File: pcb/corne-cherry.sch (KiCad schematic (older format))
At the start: 146 parts, among them J1 MJ-4PP-9, J2 OLED, J3 MJ-4PP-9, J4 OLED, J5 Conn_01x01_Male, J6 Conn_01x01_Male, P1 Conn_01x03, P3 Conn_01x03, SW1 SW_PUSH, SW10 SW_PUSH, SW11 SW_PUSH, SW12 SW_PUSH, SW13 SW_PUSH, SW14 SW_PUSH, SW15 SW_PUSH, SW16 SW_PUSH, SW17 SW_PUSH, SW18 SW_PUSH, SW19 SW_PUSH, SW2 SW_PUSH, SW20 SW_PUSH, SW21 SW_PUSH, SW22 SW_PUSH, SW23 SW_PUSH, SW24 SW_PUSH, SW25 SW_PUSH, SW26 SW_PUSH, SW27 SW_PUSH, SW28 SW_PUSH, SW29 SW_PUSH, SW3 SW_PUSH, SW30 SW_PUSH, SW31 SW_PUSH, SW32 SW_PUSH, SW33 SW_PUSH, SW34 SW_PUSH, SW35 SW_PUSH, SW36 SW_PUSH, SW37 SW_PUSH, SW38 SW_PUSH, SW39 SW_PUSH, SW4 SW_PUSH, SW40 SW_PUSH, SW41 SW_PUSH, SW42 SW_PUSH, SW43 Rotary_Encoder_Switch, SW44 Rotary_Encoder_Switch, SW5 SW_PUSH, SW6 SW_PUSH, SW7 SW_PUSH, SW8 SW_PUSH, SW9 SW_PUSH, U1 ProMicro, U2 ProMicro

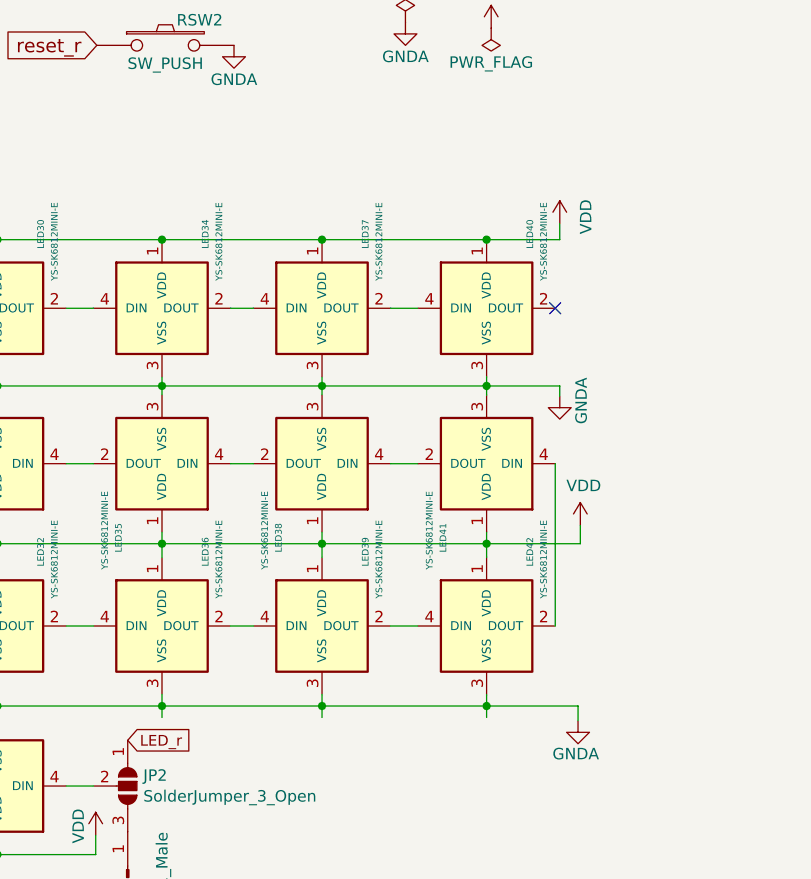
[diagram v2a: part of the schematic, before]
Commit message: Clean up schematic
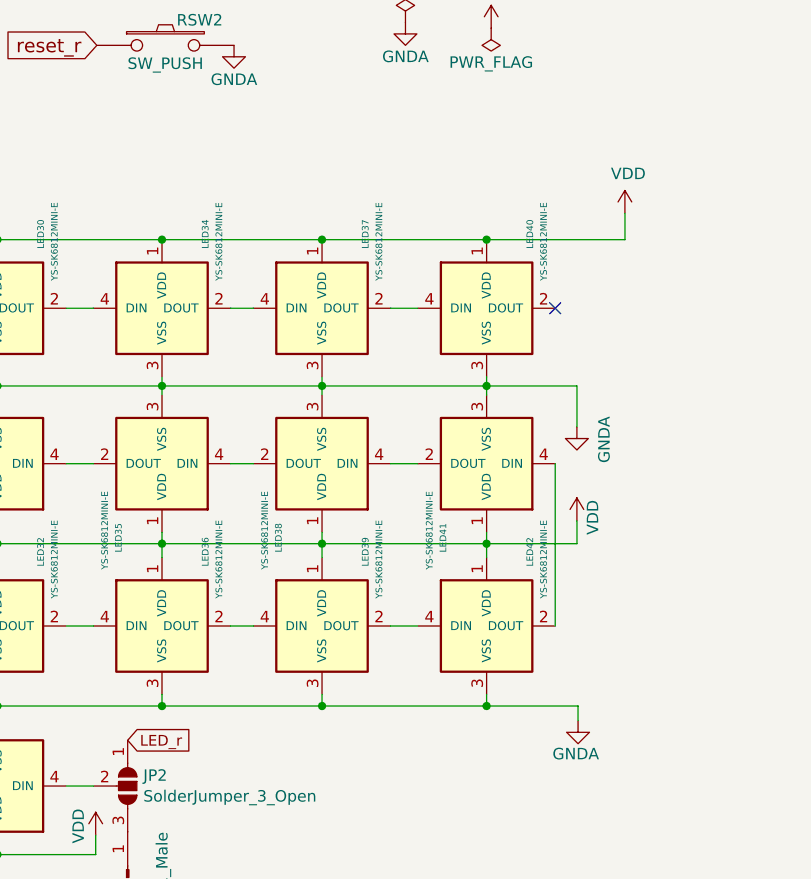
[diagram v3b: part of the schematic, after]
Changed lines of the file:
@@
 Wire Wire Line
 	7930 5730 7810 5730
-NoConn ~ 11380 5050
 $Comp
 L Connector:Conn_01x01_Male J6
@@
 Connection ~ 11080 5390
 Wire Wire Line
-	11080 5390 11400 5390
-Wire Wire Line
 	11080 5430 11080 5390
 Wire Wire Line
@@
 	8230 6790 7510 6790
 Wire Wire Line
-	11080 6840 11080 6790
-Wire Wire Line
 	11080 6740 11080 6790
 Connection ~ 11080 6790
@@
 Connection ~ 11080 6080
 Wire Wire Line
-	11080 6080 11490 6080
-Wire Wire Line
 	11080 6140 11080 6080
 Wire Wire Line
@@
 Wire Wire Line
 	10360 6080 11080 6080
-Wire Wire Line
-	10360 6840 10360 6790
 Connection ~ 10360 6790
 Wire Wire Line
@@
 Wire Wire Line
 	9960 6440 10060 6440
-Wire Wire Line
-	9660 6840 9660 6790
 Connection ~ 9660 6790
 Wire Wire Line
@@
 Wire Wire Line
 	9240 7140 9360 7140
-$Comp
-L power:VDD #PWR0112
-U 1 1 60837821
-P 11490 6000
-F 0 "#PWR0112" H 11490 5850 50  0001 C CNN
-F 1 "VDD" H 11505 6173 50  0000 C CNN
-F 2 "" H 11490 6000 50  0001 C CNN
-F 3 "" H 11490 6000 50  0001 C CNN
-	1    11490 6000
-	1    0    0    -1
-$EndComp
 $Comp
 L power:GNDA #PWR0115
@@
 	0    1    1    0
 $EndComp
-$Comp
-L power:VDD #PWR0114
-U 1 1 60838250
-P 11400 4680
-F 0 "#PWR0114" H 11400 4530 50  0001 C CNN
-F 1 "VDD" V 11515 4710 50  0000 C CNN
-F 2 "" H 11400 4680 50  0001 C CNN
-F 3 "" H 11400 4680 50  0001 C CNN
-	1    11400 4680
-	1    0    0    -1
-$EndComp
 Wire Wire Line
 	5360 7410 5360 7325
@@
 Wire Wire Line
 	11480 6855 11480 6790
-Wire Wire Line
-	11490 6080 11490 6000
-Connection ~ 11080 4750
-Wire Wire Line
-	11080 4750 11400 4750
+$Comp
+L Device:Rotary_Encoder_Switch SW43
+U 1 1 6078866B
+P 3135 785
+F 0 "SW43" V 3089 1015 50  0000 L CNN
+F 1 "Rotary_Encoder_Switch" V 3180 1015 50  0000 L CNN
+F 2 "Keebio-Parts:RotaryEncoder_EC11-no-legs" H 2985 945 50  0001 C CNN
+F 3 "~" H 3135 1045 50  0001 C CNN
+	1    3135 785
+	1    0    0    -1
+$EndComp
+Wire Wire Line
+	2835 785  2420 785
+Wire Wire Line
+	2420 785  2420 885
+$Comp
+L power:GND #PWR0119
+U 1 1 60823858
+P 2420 885
+F 0 "#PWR0119" H 2420 635 50  0001 C CNN
+F 1 "GND" H 2425 712 50  0000 C CNN
+F 2 "" H 2420 885 50  0001 C CNN
+F 3 "" H 2420 885 50  0001 C CNN
+	1    2420 885
+	1    0    0    -1
+$EndComp
+Text GLabel 2835 685  0    50   Input ~ 0
+ENC_A
+Text GLabel 2835 885  0    50   Input ~ 0
+ENC_B
+Text GLabel 2475 2275 2    50   Input ~ 0
+ENC_B
+Text GLabel 2475 2175 2    50   Input ~ 0
+ENC_A
+Wire Wire Line
+	3435 885  3435 1275
+Wire Wire Line
+	3435 1275 3600 1275
+Connection ~ 3600 1275
+Wire Wire Line
+	3600 1275 3600 2475
+Wire Wire Line
+	3435 685  4200 685
+Wire Wire Line
+	4200 685  4200 1275
+Connection ~ 4200 1275
+Text GLabel 9905 2150 2    50   Input ~ 0
+ENC_A_R
+Text GLabel 9905 2250 2    50   Input ~ 0
+ENC_B_R
+$Comp
+L Device:Rotary_Encoder_Switch SW44
+U 1 1 60786552
+P 11045 930
+F 0 "SW44" H 11045 1297 50  0000 C CNN
+F 1 "Rotary_Encoder_Switch" H 11045 1206 50  0000 C CNN
+F 2 "Keebio-Parts:RotaryEncoder_EC11-no-legs" H 10895 1090 50  0001 C CNN
+F 3 "~" H 11045 1190 50  0001 C CNN
+	1    11045 930
+	1    0    0    -1
+$EndComp
+Text GLabel 10745 1030 0    50   Input ~ 0
+ENC_B_R
+Text GLabel 10745 830  0    50   Input ~ 0
+ENC_A_R
+Wire Wire Line
+	10745 930  10150 930
+Wire Wire Line
+	10150 930  10150 1030
+$Comp
+L power:GNDA #PWR0120
+U 1 1 607DCD43
+P 10150 1030
+F 0 "#PWR0120" H 10150 780 50  0001 C CNN
+F 1 "GNDA" V 10060 1020 50  0000 C CNN
+F 2 "" H 10150 1030 50  0001 C CNN
+F 3 "" H 10150 1030 50  0001 C CNN
+	1    10150 1030
+	1    0    0    -1
+$EndComp
+Wire Wire Line
+	11345 830  12175 830
+Wire Wire Line
+	12175 830  12175 1400
+Connection ~ 12175 1400
+Wire Wire Line
+	11345 1030 11345 1400
+Wire Wire Line
+	11345 1400 11575 1400
+Connection ~ 11575 1400
+Wire Wire Line
+	11575 1400 11575 2600
 Wire Wire Line
 	10360 4750 11080 4750
@@
 	1    0    0    -1
 $EndComp
-$Comp
-L power:GNDA #PWR0116
-U 1 1 6087A621
-P 11400 5435
-F 0 "#PWR0116" H 11400 5185 50  0001 C CNN
-F 1 "GNDA" V 11495 5415 50  0000 C CNN
-F 2 "" H 11400 5435 50  0001 C CNN
-F 3 "" H 11400 5435 50  0001 C CNN
-	1    11400 5435
-	1    0    0    -1
-$EndComp
-Wire Wire Line
-	11400 5390 11400 5435
-Wire Wire Line
-	11400 4750 11400 4680
-$Comp
-L Device:Rotary_Encoder_Switch SW43
-U 1 1 6078866B
-P 3135 785
-F 0 "SW43" V 3089 1015 50  0000 L CNN
-F 1 "Rotary_Encoder_Switch" V 3180 1015 50  0000 L CNN
-F 2 "Keebio-Parts:RotaryEncoder_EC11-no-legs" H 2985 945 50  0001 C CNN
-F 3 "~" H 3135 1045 50  0001 C CNN
-	1    3135 785
-	1    0    0    -1
-$EndComp
-Wire Wire Line
-	2835 785  2420 785
-Wire Wire Line
-	2420 785  2420 885
-$Comp
-L power:GND #PWR0119
-U 1 1 60823858
-P 2420 885
-F 0 "#PWR0119" H 2420 635 50  0001 C CNN
-F 1 "GND" H 2425 712 50  0000 C CNN
-F 2 "" H 2420 885 50  0001 C CNN
-F 3 "" H 2420 885 50  0001 C CNN
-	1    2420 885
-	1    0    0    -1
-$EndComp
-Text GLabel 2835 685  0    50   Input ~ 0
-ENC_A
-Text GLabel 2835 885  0    50   Input ~ 0
-ENC_B
-Text GLabel 2475 2275 2    50   Input ~ 0
-ENC_B
-Text GLabel 2475 2175 2    50   Input ~ 0
-ENC_A
-Wire Wire Line
-	3435 885  3435 1275
-Wire Wire Line
-	3435 1275 3600 1275
-Connection ~ 3600 1275
-Wire Wire Line
-	3600 1275 3600 2475
-Wire Wire Line
-	3435 685  4200 685
-Wire Wire Line
-	4200 685  4200 1275
-Connection ~ 4200 1275
-Text GLabel 9905 2150 2    50   Input ~ 0
-ENC_A_R
-Text GLabel 9905 2250 2    50   Input ~ 0
-ENC_B_R
-$Comp
-L Device:Rotary_Encoder_Switch SW44
-U 1 1 60786552
-P 11045 930
-F 0 "SW44" H 11045 1297 50  0000 C CNN
-F 1 "Rotary_Encoder_Switch" H 11045 1206 50  0000 C CNN
-F 2 "Keebio-Parts:RotaryEncoder_EC11-no-legs" H 10895 1090 50  0001 C CNN
-F 3 "~" H 11045 1190 50  0001 C CNN
-	1    11045 930
-	1    0    0    -1
-$EndComp
-Text GLabel 10745 1030 0    50   Input ~ 0
-ENC_B_R
-Text GLabel 10745 830  0    50   Input ~ 0
-ENC_A_R
-Wire Wire Line
-	10745 930  10150 930
-Wire Wire Line
-	10150 930  10150 1030
-$Comp
-L power:GNDA #PWR0120
-U 1 1 607DCD43
-P 10150 1030
-F 0 "#PWR0120" H 10150 780 50  0001 C CNN
-F 1 "GNDA" V 10060 1020 50  0000 C CNN
-F 2 "" H 10150 1030 50  0001 C CNN
-F 3 "" H 10150 1030 50  0001 C CNN
-	1    10150 1030
-	1    0    0    -1
-$EndComp
-Wire Wire Line
-	11345 830  12175 830
-Wire Wire Line
-	12175 830  12175 1400
-Connection ~ 12175 1400
-Wire Wire Line
-	11345 1030 11345 1400
-Wire Wire Line
-	11345 1400 11575 1400
-Connection ~ 11575 1400
-Wire Wire Line
-	11575 1400 11575 2600
+NoConn ~ 11380 5050
+Wire Wire Line
+	11080 6080 11475 6080
+Wire Wire Line
+	11475 6080 11475 5980
+$Comp
+L power:VDD #PWR0112
+U 1 1 60DCBB52
+P 11475 5980
+F 0 "#PWR0112" H 11475 5830 50  0001 C CNN
+F 1 "VDD" V 11545 5995 50  0000 C CNN
+F 2 "" H 11475 5980 50  0001 C CNN
+F 3 "" H 11475 5980 50  0001 C CNN
+	1    11475 5980
+	1    0    0    -1
+$EndComp
+Wire Wire Line
+	11080 5390 11475 5390
+Wire Wire Line
+	11475 5390 11475 5570
+$Comp
+L power:GNDA #PWR0114
+U 1 1 60DF6BE8
+P 11475 5570
+F 0 "#PWR0114" H 11475 5320 50  0001 C CNN
+F 1 "GNDA" V 11595 5515 50  0000 C CNN
+F 2 "" H 11475 5570 50  0001 C CNN
+F 3 "" H 11475 5570 50  0001 C CNN
+	1    11475 5570
+	1    0    0    -1
+$EndComp
+Wire Wire Line
+	11080 4750 11685 4750
+Wire Wire Line
+	11685 4750 11685 4635
+Connection ~ 11080 4750
+$Comp
+L power:VDD #PWR0116
+U 1 1 60E14086
+P 11685 4635
+F 0 "#PWR0116" H 11685 4485 50  0001 C CNN
+F 1 "VDD" H 11700 4808 50  0000 C CNN
+F 2 "" H 11685 4635 50  0001 C CNN
+F 3 "" H 11685 4635 50  0001 C CNN
+	1    11685 4635
+	1    0    0    -1
+$EndComp
 $EndSCHEMATC

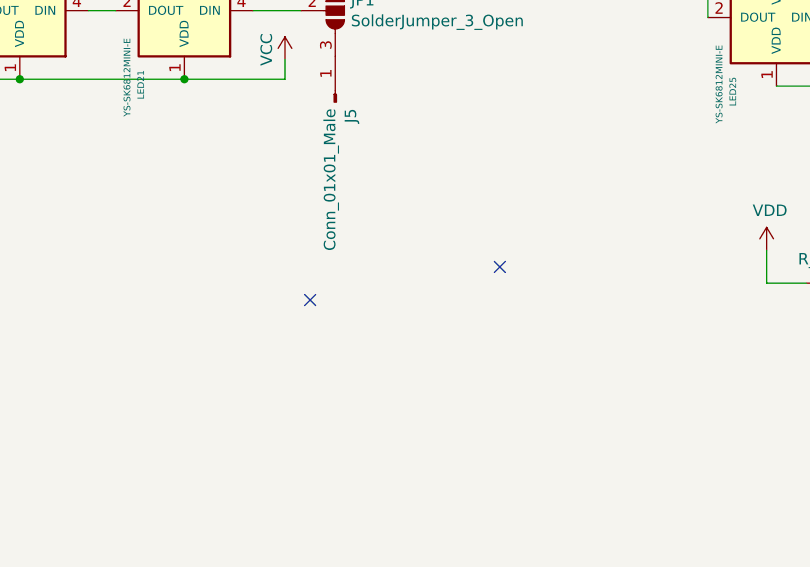
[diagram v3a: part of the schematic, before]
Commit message: change trace position - too close too mousebites
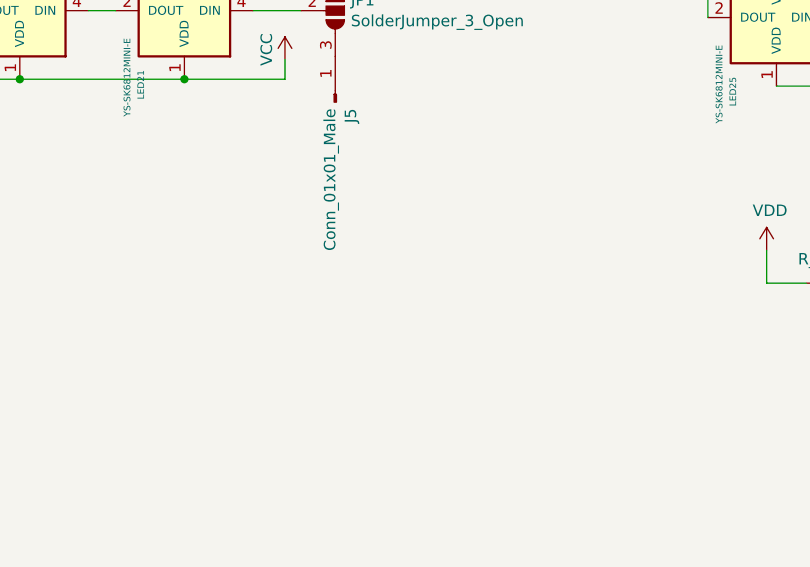
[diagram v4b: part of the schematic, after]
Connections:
- no-connect marks 11 -> 9
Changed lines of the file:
@@
 $EndComp
 NoConn ~ 5718 9687
-NoConn ~ 5470 8376
-NoConn ~ 6300 8231
 Text GLabel 5550 4150 0    47   Input ~ 0
 LED

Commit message: Silkscreen stuff on PCB and clean up schematiccm
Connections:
- net col0: now also SW7.1
- net col0_r: now also SW28.1
- net col1: now also SW2.1, SW8.1
- net col1_r: now also SW23.1, SW29.1
- net col2: now also SW3.1, SW9.1
- net col2_r: now also SW24.1, SW30.1
- net col3: now also SW10.1, SW16.1, SW4.1
- net col3_r: now also SW25.1, SW31.1, SW37.1
- net col4: now also SW11.1, SW17.1, SW5.1
- net col4_r: now also SW26.1, SW32.1, SW38.1
- net col5: now also SW12.1, SW18.1, SW6.1
- net col5_r: now also SW27.1, SW33.1, SW39.1
- no-connect marks 9 -> 8
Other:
- note added: "Controllers"
- note added: "Misc"
- note added: "RGB"
- note added: "Switch Matrix"
- moved on the sheet: D1, D10, D11, D12, D13, D14, D15, D16, D17, D18, D19, D2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
